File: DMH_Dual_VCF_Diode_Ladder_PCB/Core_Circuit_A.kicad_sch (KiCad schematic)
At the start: 52 parts, among them SW1 SW_SPDT, SW2 SW_SPDT, SW3 SW_SPDT, SW5 SW_SP3T, U1 TL074, U2 TL074

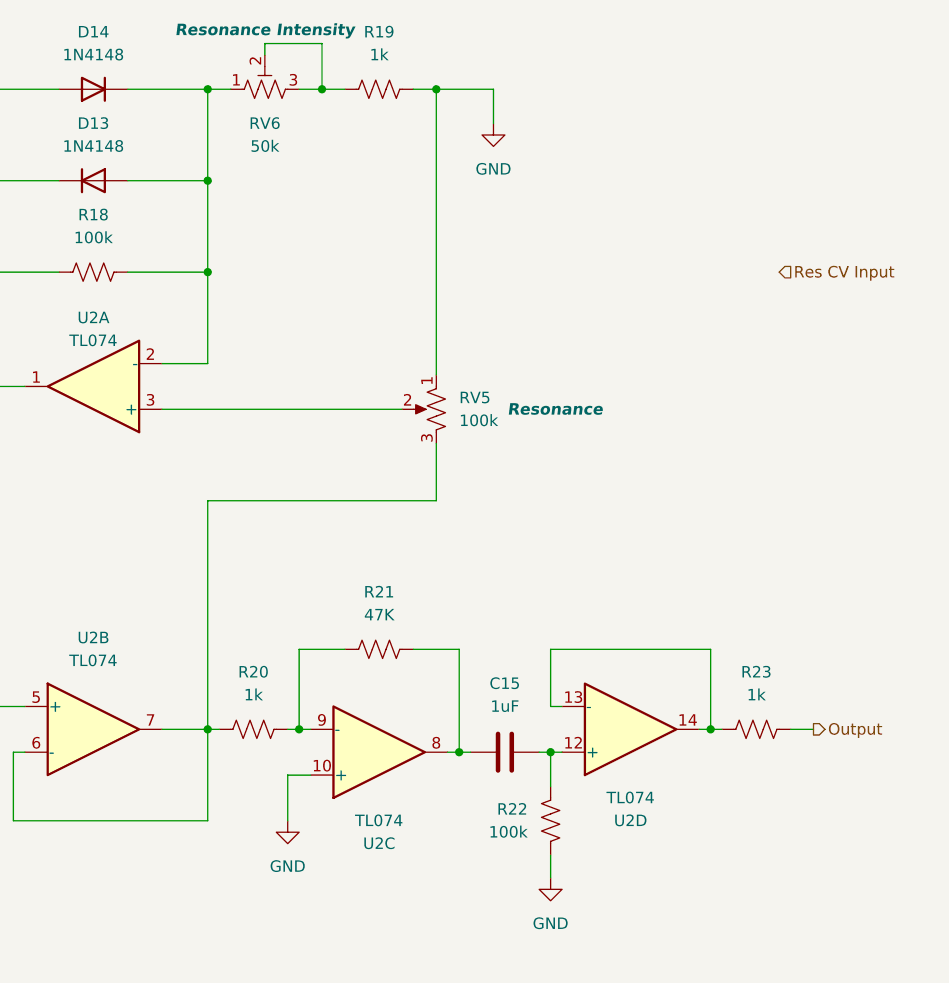
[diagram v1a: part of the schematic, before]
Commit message: Starting Res CV design
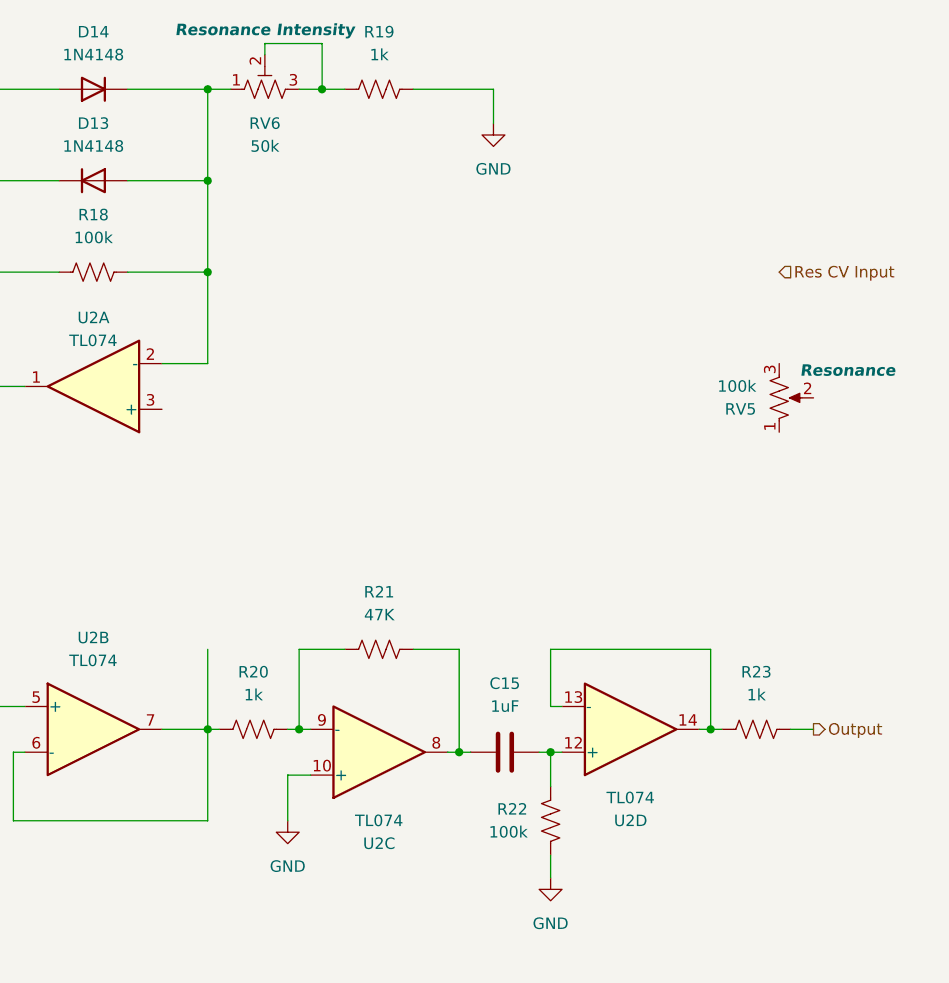
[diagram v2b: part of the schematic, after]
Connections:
- net GND: no longer RV5.1
- net at U2.3 (+): no longer RV5.2
- net at R20.1, U2.6 (-), U2.7: no longer RV5.3
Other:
- moved on the sheet: RV5
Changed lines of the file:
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@@
 	)
 	(junction
-		(at 228.6 30.48)
-		(diameter 0)
-		(color 0 0 0 0)
-	)
-	(junction
 		(at 177.8 40.64)
 		(diameter 0)
@@
 	(wire
 		(pts
-			(xy 228.6 30.48) (xy 234.95 30.48)
-		)
-		(stroke
-			(width 0)
-			(type default)
-		)
-	)
-	(wire
-		(pts
 			(xy 203.2 40.64) (xy 203.2 50.8)
 		)
@@
 	(wire
 		(pts
-			(xy 228.6 69.85) (xy 228.6 76.2)
-		)
-		(stroke
-			(width 0)
-			(type default)
-		)
-	)
-	(wire
-		(pts
 			(xy 78.74 152.4) (xy 81.28 152.4)
 		)
@@
 	(wire
 		(pts
-			(xy 203.2 111.76) (xy 203.2 101.6)
-		)
-		(stroke
-			(width 0)
-			(type default)
-		)
-	)
-	(wire
-		(pts
 			(xy 74.93 58.42) (xy 74.93 46.99)
 		)
@@
 	(wire
 		(pts
-			(xy 52.07 101.6) (xy 54.61 101.6)
+			(xy 226.06 30.48) (xy 234.95 30.48)
 		)
 		(stroke
@@
 	(wire
 		(pts
-			(xy 124.46 76.2) (xy 127 76.2)
+			(xy 52.07 101.6) (xy 54.61 101.6)
 		)
 		(stroke
@@
 	(wire
 		(pts
-			(xy 104.14 60.96) (xy 106.68 60.96)
+			(xy 124.46 76.2) (xy 127 76.2)
 		)
 		(stroke
@@
 	(wire
 		(pts
-			(xy 88.9 162.56) (xy 91.44 162.56)
+			(xy 104.14 60.96) (xy 106.68 60.96)
 		)
 		(stroke
@@
 	(wire
 		(pts
-			(xy 198.12 66.04) (xy 224.79 66.04)
+			(xy 88.9 162.56) (xy 91.44 162.56)
 		)
 		(stroke
@@
 	(wire
 		(pts
-			(xy 228.6 76.2) (xy 203.2 76.2)
+			(xy 203.2 101.6) (xy 203.2 111.76)
 		)
 		(stroke
@@
 	(wire
 		(pts
-			(xy 228.6 30.48) (xy 228.6 62.23)
-		)
-		(stroke
-			(width 0)
-			(type default)
-		)
-	)
-	(wire
-		(pts
 			(xy 177.8 63.5) (xy 177.8 73.66)
 		)
@@
 	(wire
 		(pts
-			(xy 226.06 30.48) (xy 228.6 30.48)
-		)
-		(stroke
-			(width 0)
-			(type default)
-		)
-	)
-	(wire
-		(pts
-			(xy 203.2 76.2) (xy 203.2 101.6)
+			(xy 203.2 92.71) (xy 203.2 101.6)
 		)
 		(stroke
@@
 	(symbol
 		(lib_id "Device:R_Potentiometer_US")
-		(at 228.6 66.04 0)
-		(mirror y)
+		(at 266.7 64.77 0)
+		(mirror x)
 		(unit 1)
 		(exclude_from_sim no)
@@
 		(dnp no)
 		(property "Reference" "RV5"
-			(at 231.14 64.7699 0)
+			(at 264.16 66.0401 0)
 			(effects
 				(font
@@
 		)
 		(property "Value" "100k"
-			(at 231.14 67.3099 0)
+			(at 264.16 63.5001 0)
 			(effects
 				(font
@@
 		)
 		(property "Footprint" "SynthStuff:Potentiometer_Alpha_RD901F-40-00D_Single_Vertical"
-			(at 228.6 66.04 0)
+			(at 266.7 64.77 0)
 			(effects
 				(font
@@
 		)
 		(property "Datasheet" "~"
-			(at 228.6 66.04 0)
+			(at 266.7 64.77 0)
 			(effects
 				(font
@@
 		)
 		(property "Description" "Potentiometer, US symbol"
-			(at 228.6 66.04 0)
+			(at 266.7 64.77 0)
 			(effects
 				(font
@@
 		)
 		(property "Function" "Resonance"
-			(at 241.808 66.04 0)
+			(at 274.32 61.722 0)
 			(effects
 				(font

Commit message: Generated BoM
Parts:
- RV3, RV4, RV5: footprint SynthStuff:Potentiometer_Alpha_RD901F-40-00D_Single_Vertical -> SynthStuff:Potentiometer_TT_P110KH1
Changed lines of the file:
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@@
 			)
 		)
-		(property "Footprint" "SynthStuff:Potentiometer_Alpha_RD901F-40-00D_Single_Vertical"
+		(property "Footprint" "SynthStuff:Potentiometer_TT_P110KH1"
 			(at 38.1 160.02 0)
 			(effects
@@
 			)
 		)
-		(property "Footprint" "SynthStuff:Potentiometer_Alpha_RD901F-40-00D_Single_Vertical"
+		(property "Footprint" "SynthStuff:Potentiometer_TT_P110KH1"
 			(at 38.1 134.62 0)
 			(effects
@@
 			)
 		)
-		(property "Footprint" "SynthStuff:Potentiometer_Alpha_RD901F-40-00D_Single_Vertical"
+		(property "Footprint" "SynthStuff:Potentiometer_TT_P110KH1"
 			(at 266.7 64.77 0)
 			(effects
